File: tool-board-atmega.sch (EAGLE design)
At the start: 84 parts, among them IC3 ATMEGA2560-16AU, IC4 ATMEGA8U2-MU, Q1 16MHz, X1 22-23-2041, X2 MICROUSB_VERTICAL, X3 22-23-2041, X4 22-23-2041, Y2 16MHz

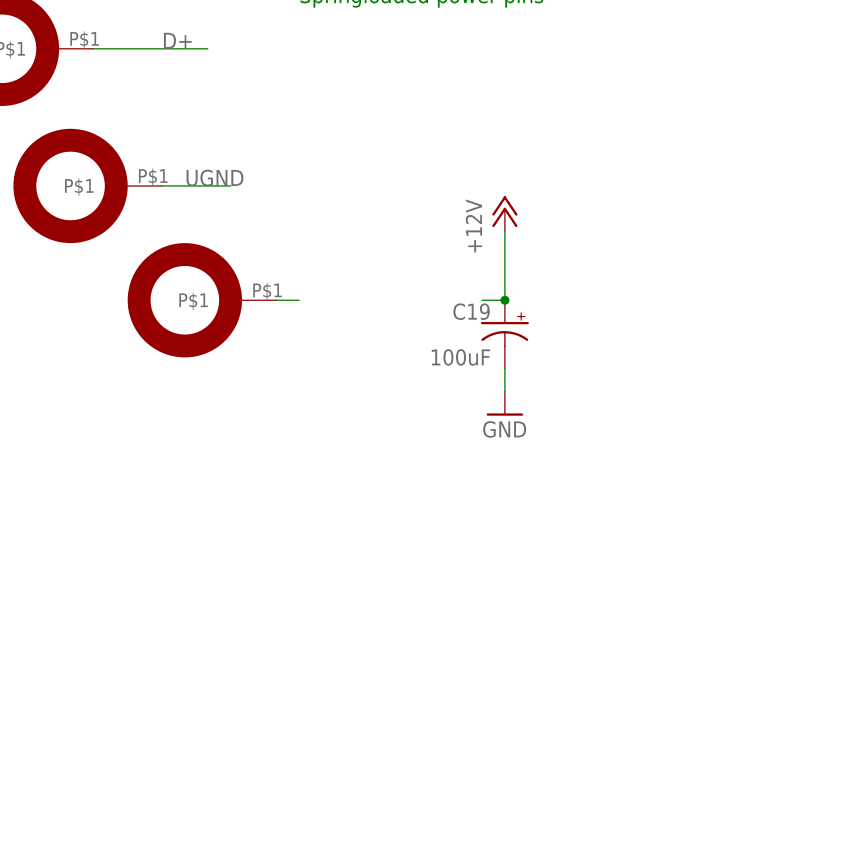
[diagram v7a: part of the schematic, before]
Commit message: polys poured, local power vias placed
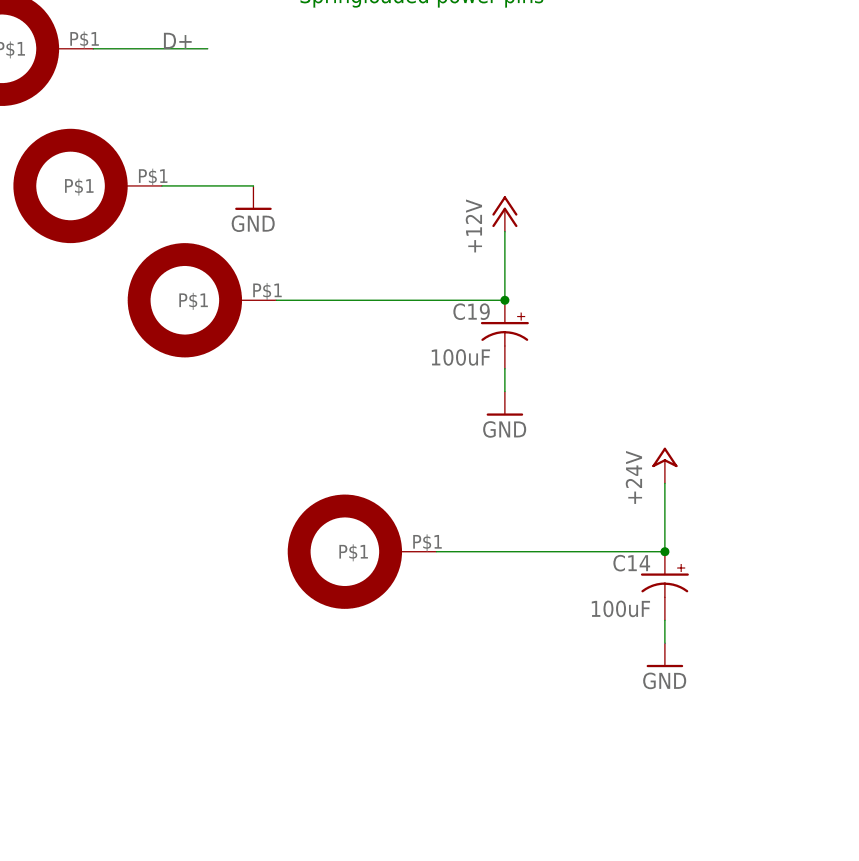
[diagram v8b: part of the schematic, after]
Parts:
- added C14: 100uF, rcl:CPOL-USE3.5-8
- added U$6: SPRING_CONTACT, ClinicalRobotics:SPRING_CONTACT
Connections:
- new net +24V: C14.+, U$6.P$1
- net +12V: now also U$12.P$1
- net +12VIN: no longer U$12.P$1
- net GND: now also C14.-, U$11.P$1
- net UGND: no longer U$11.P$1
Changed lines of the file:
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@@
 <part name="X3" library="con-molex" library_urn="urn:adsk.eagle:library:165" deviceset="22-23-2041" device="" package3d_urn="urn:adsk.eagle:package:8078635/1"/>
 <part name="X4" library="con-molex" library_urn="urn:adsk.eagle:library:165" deviceset="22-23-2041" device="" package3d_urn="urn:adsk.eagle:package:8078635/1"/>
+<part name="U$6" library="ClinicalRobotics" deviceset="SPRING_CONTACT" device=""/>
+<part name="C14" library="rcl" library_urn="urn:adsk.eagle:library:334" deviceset="CPOL-US" device="E3.5-8" package3d_urn="urn:adsk.eagle:package:23360/2" value="100uF"/>
+<part name="GND20" library="supply1" deviceset="GND" device=""/>
+<part name="P+7" library="supply1" library_urn="urn:adsk.eagle:library:371" deviceset="+24V" device=""/>
+<part name="GND27" library="supply1" deviceset="GND" device=""/>
 </parts>
 <sheets>
@@
 <attribute name="NAME" x="-12.7" y="4.318" size="1.524" layer="95"/>
 </instance>
+<instance part="U$6" gate="G$1" x="421.64" y="-111.76" smashed="yes" rot="R180"/>
+<instance part="C14" gate="G$1" x="457.2" y="-114.3" smashed="yes" rot="MR0">
+<attribute name="NAME" x="455.676" y="-113.919" size="1.778" layer="95" rot="MR0"/>
+<attribute name="VALUE" x="455.676" y="-118.999" size="1.778" layer="96" rot="MR0"/>
+</instance>
+<instance part="GND20" gate="1" x="457.2" y="-124.46" smashed="yes">
+<attribute name="VALUE" x="454.66" y="-127" size="1.778" layer="96"/>
+</instance>
+<instance part="P+7" gate="1" x="457.2" y="-101.6" smashed="yes">
+<attribute name="VALUE" x="454.66" y="-106.68" size="1.778" layer="96" rot="R90"/>
+</instance>
+<instance part="GND27" gate="1" x="411.48" y="-73.66" smashed="yes">
+<attribute name="VALUE" x="408.94" y="-76.2" size="1.778" layer="96"/>
+</instance>
 </instances>
 <busses>
@@
 <wire x1="431.8" y1="-33.02" x2="431.8" y2="-35.56" width="0.1524" layer="91"/>
 </segment>
+<segment>
+<pinref part="GND20" gate="1" pin="GND"/>
+<pinref part="C14" gate="G$1" pin="-"/>
+<wire x1="457.2" y1="-121.92" x2="457.2" y2="-119.38" width="0.1524" layer="91"/>
+</segment>
+<segment>
+<pinref part="U$11" gate="G$1" pin="P$1"/>
+<wire x1="401.32" y1="-71.12" x2="411.48" y2="-71.12" width="0.1524" layer="91"/>
+<pinref part="GND27" gate="1" pin="GND"/>
+</segment>
 </net>
 <net name="AREF" class="0">
@@
 <junction x="368.3" y="38.1"/>
 </segment>
-<segment>
-<pinref part="U$11" gate="G$1" pin="P$1"/>
-<wire x1="401.32" y1="-71.12" x2="408.94" y2="-71.12" width="0.1524" layer="91"/>
-<label x="403.86" y="-71.12" size="1.778" layer="95"/>
-</segment>
 </net>
 <net name="XT2" class="0">
@@
 <wire x1="190.5" y1="-116.84" x2="180.34" y2="-116.84" width="0.1524" layer="91"/>
 <label x="182.88" y="-116.84" size="1.778" layer="95"/>
-</segment>
-<segment>
-<pinref part="U$12" gate="G$1" pin="P$1"/>
-<wire x1="414.02" y1="-83.82" x2="416.56" y2="-83.82" width="0.1524" layer="91"/>
 </segment>
 </net>
@@
 <segment>
 <pinref part="P+15" gate="1" pin="+12V"/>
-<wire x1="436.88" y1="-83.82" x2="439.42" y2="-83.82" width="0.1524" layer="91"/>
 <wire x1="439.42" y1="-83.82" x2="439.42" y2="-76.2" width="0.1524" layer="91"/>
 <pinref part="C19" gate="G$1" pin="+"/>
 <junction x="439.42" y="-83.82"/>
+<pinref part="U$12" gate="G$1" pin="P$1"/>
+<wire x1="414.02" y1="-83.82" x2="439.42" y2="-83.82" width="0.1524" layer="91"/>
 </segment>
 <segment>
@@
 </segment>
 </net>
+<net name="+24V" class="0">
+<segment>
+<wire x1="457.2" y1="-111.76" x2="457.2" y2="-104.14" width="0.1524" layer="91"/>
+<pinref part="C14" gate="G$1" pin="+"/>
+<junction x="457.2" y="-111.76"/>
+<pinref part="U$6" gate="G$1" pin="P$1"/>
+<wire x1="431.8" y1="-111.76" x2="457.2" y2="-111.76" width="0.1524" layer="91"/>
+<pinref part="P+7" gate="1" pin="+24V"/>
+</segment>
+</net>
